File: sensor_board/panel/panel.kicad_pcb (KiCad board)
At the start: 2 copper layers, 102.6 x 105.2 mm, 132 parts, among them J1 Comm, J2 OUTPUT, J3 INPUT, U1 INA228

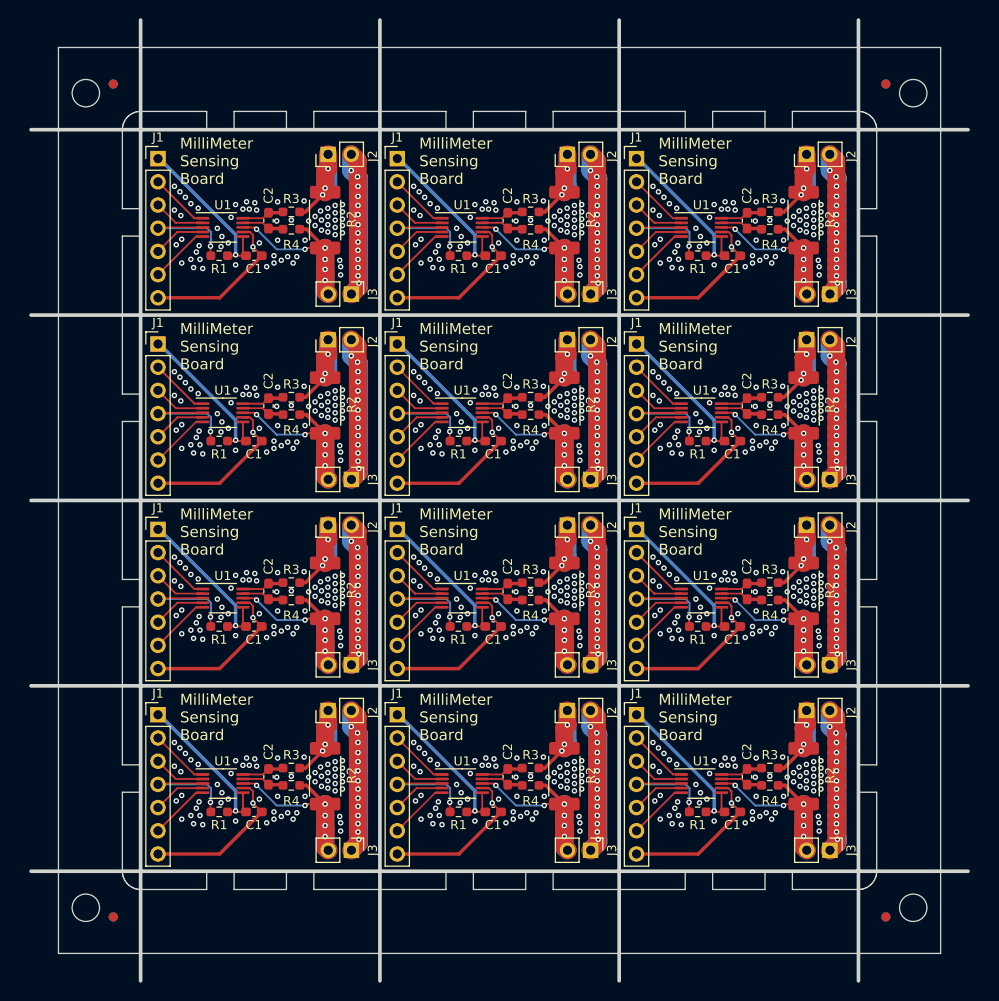
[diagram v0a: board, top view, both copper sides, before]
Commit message: sensor_board: rev 1.1
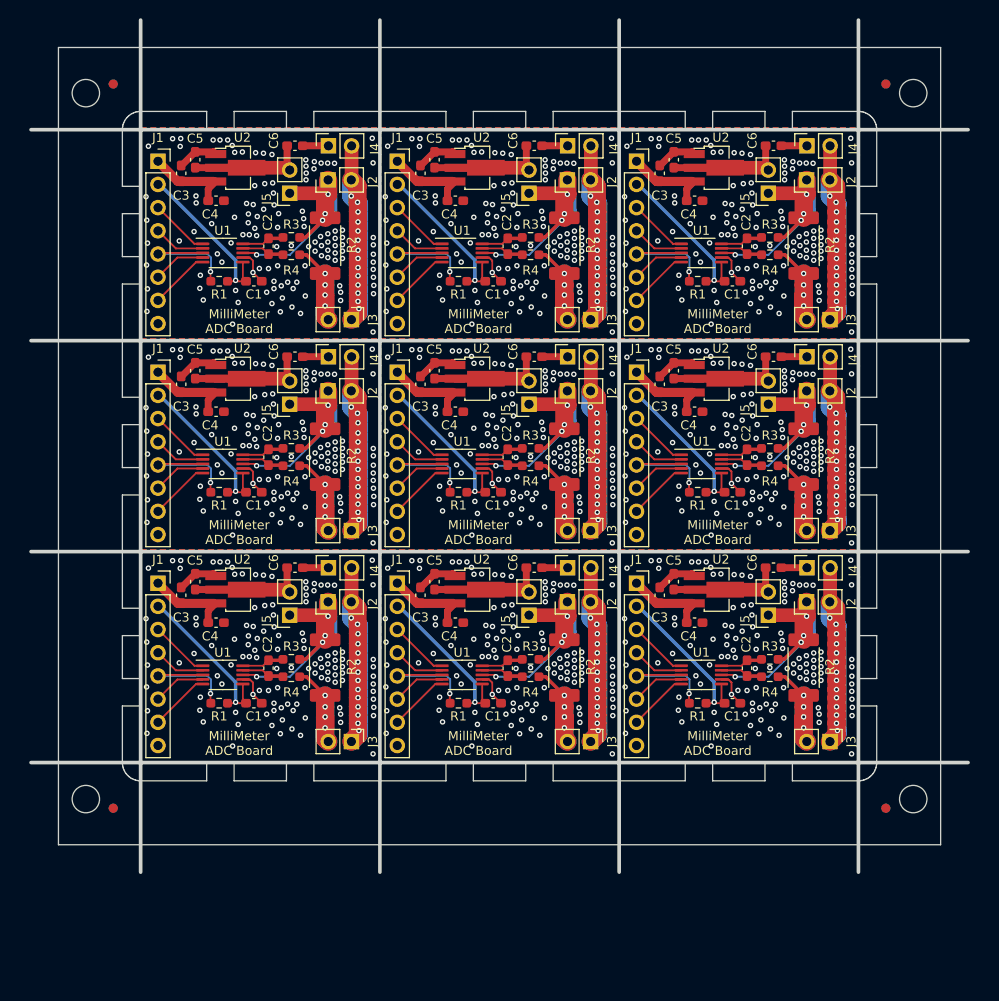
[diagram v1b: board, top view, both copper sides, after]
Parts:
- removed the C1 at (174.0, 63.1)
- removed the C1 at (174.0, 103.7)
- removed the C1 at (147.8, 42.8)
- removed the C1 at (174.0, 42.8)
- removed the C1 at (174.0, 83.4)
- removed the C1 at (121.6, 42.8)
- removed the C1 at (147.8, 83.4)
- removed the C1 at (121.6, 83.4)
- removed the C1 at (147.8, 103.7)
- removed the C1 at (147.8, 63.1)
- removed the C1 at (121.6, 63.1)
- removed the C1 at (121.6, 103.7)
- removed the C2 at (149.4, 99.9)
- removed the C2 at (123.2, 39.0)
- removed the C2 at (123.2, 99.9)
- removed the C2 at (149.4, 39.0)
- removed the C2 at (123.2, 59.3)
- removed the C2 at (175.6, 79.6)
- removed the C2 at (175.6, 39.0)
- removed the C2 at (149.4, 79.6)
- removed the C2 at (175.6, 59.3)
- removed the C2 at (175.6, 99.9)
- removed the C2 at (149.4, 59.3)
- removed the C2 at (123.2, 79.6)
- removed the J1 at (137.3, 72.8)
- removed the J1 at (163.5, 93.1)
- removed the J1 at (137.3, 32.2)
- removed the J1 at (163.5, 32.2)
- removed the J1 at (163.5, 72.8)
- removed the J1 at (111.1, 32.2)
- removed the J1 at (137.3, 52.5)
- removed the J1 at (137.3, 93.1)
- removed the J1 at (163.5, 52.5)
- removed the J1 at (111.1, 72.8)
- removed the J1 at (111.1, 93.1)
- removed the J1 at (111.1, 52.5)
- removed the J2 at (182.1, 92.6)
- removed the J2 at (129.7, 52.0)
- removed the J2 at (155.9, 52.0)
- removed the J2 at (182.1, 72.3)
- removed the J2 at (182.1, 52.0)
- removed the J2 at (155.9, 72.3)
- removed the J2 at (129.7, 31.7)
- removed the J2 at (155.9, 92.6)
- removed the J2 at (129.7, 92.6)
- removed the J2 at (182.1, 31.7)
- removed the J2 at (155.9, 31.7)
- removed the J2 at (129.7, 72.3)
- removed the J3 at (132.3, 87.6)
- removed the J3 at (184.7, 87.6)
- removed the J3 at (184.7, 47.0)
- removed the J3 at (184.7, 67.3)
- removed the J3 at (132.3, 107.9)
- removed the J3 at (158.5, 87.6)
- removed the J3 at (184.7, 107.9)
- removed the J3 at (158.5, 107.9)
- removed the J3 at (132.3, 67.3)
- removed the J3 at (132.3, 47.0)
- removed the J3 at (158.5, 67.3)
- removed the J3 at (158.5, 47.0)
- removed the R1 at (170.2, 63.1)
- removed the R1 at (117.8, 83.4)
- removed the R1 at (170.2, 103.7)
- removed the R1 at (144.0, 103.7)
- removed the R1 at (117.8, 63.1)
- removed the R1 at (170.2, 83.4)
- removed the R1 at (144.0, 42.8)
- removed the R1 at (117.8, 42.8)
- removed the R1 at (170.2, 42.8)
- removed the R1 at (144.0, 63.1)
- removed the R1 at (144.0, 83.4)
- removed the R1 at (117.8, 103.7)
- removed the R2 at (129.4, 59.2)
- removed the R2 at (129.4, 38.9)
- removed the R2 at (155.6, 99.8)
- removed the R2 at (181.8, 38.9)
- removed the R2 at (155.6, 59.2)
- removed the R2 at (155.6, 79.5)
- removed the R2 at (181.8, 79.5)
- removed the R2 at (181.8, 59.2)
- removed the R2 at (155.6, 38.9)
- removed the R2 at (129.4, 79.5)
- removed the R2 at (181.8, 99.8)
- removed the R2 at (129.4, 99.8)
- removed the R3 at (125.7, 38.0)
- removed the R3 at (125.7, 58.3)
- removed the R3 at (151.9, 78.6)
- removed the R3 at (178.1, 38.0)
- removed the R3 at (125.7, 98.9)
- removed the R3 at (125.7, 78.6)
- removed the R3 at (178.1, 98.9)
- removed the R3 at (151.9, 58.3)
- removed the R3 at (178.1, 78.6)
- removed the R3 at (151.9, 98.9)
- removed the R3 at (151.9, 38.0)
- removed the R3 at (178.1, 58.3)
- removed the R4 at (125.7, 100.8)
- removed the R4 at (178.1, 60.2)
- removed the R4 at (125.7, 80.5)
- removed the R4 at (151.9, 60.2)
- removed the R4 at (125.7, 60.2)
- removed the R4 at (178.1, 80.5)
- removed the R4 at (151.9, 80.5)
- removed the R4 at (178.1, 39.9)
- removed the R4 at (151.9, 39.9)
- removed the R4 at (178.1, 100.8)
- removed the R4 at (151.9, 100.8)
- removed the R4 at (125.7, 39.9)
- removed the REF** at (103.2, 114.2)
- removed the REF** at (106.2, 115.2) (x2)
- removed the REF** at (106.2, 24.0) (x2)
- removed the REF** at (190.8, 115.2) (x2)
- removed the REF** at (190.8, 24.0) (x2)
- removed the REF** at (193.8, 114.2)
- removed the U1 at (118.2, 100.6)
- removed the U1 at (144.4, 60.0)
- removed the U1 at (118.2, 39.7)
- removed the U1 at (118.2, 80.3)
- removed the U1 at (170.6, 60.0)
- removed the U1 at (170.6, 39.7)
- removed the U1 at (144.4, 39.7)
- removed the U1 at (170.6, 80.3)
- removed the U1 at (144.4, 100.6)
- removed the U1 at (118.2, 60.0)
- removed the U1 at (144.4, 80.3)
- removed the U1 at (170.6, 100.6)
- added C1: 100nF, Capacitor_SMD:C_0603_1608Metric_Pad1.08x0.95mm_HandSolder, F.Cu at (147.8, 68.7)
- added C1: 100nF, Capacitor_SMD:C_0603_1608Metric_Pad1.08x0.95mm_HandSolder, F.Cu at (121.6, 68.7)
- added C1: 100nF, Capacitor_SMD:C_0603_1608Metric_Pad1.08x0.95mm_HandSolder, F.Cu at (174.0, 91.8)
- added C1: 100nF, Capacitor_SMD:C_0603_1608Metric_Pad1.08x0.95mm_HandSolder, F.Cu at (174.0, 45.6)
- added C1: 100nF, Capacitor_SMD:C_0603_1608Metric_Pad1.08x0.95mm_HandSolder, F.Cu at (121.6, 91.8)
- added C1: 100nF, Capacitor_SMD:C_0603_1608Metric_Pad1.08x0.95mm_HandSolder, F.Cu at (121.6, 45.6)
- added C1: 100nF, Capacitor_SMD:C_0603_1608Metric_Pad1.08x0.95mm_HandSolder, F.Cu at (147.8, 45.6)
- added C1: 100nF, Capacitor_SMD:C_0603_1608Metric_Pad1.08x0.95mm_HandSolder, F.Cu at (174.0, 68.7)
- added C1: 100nF, Capacitor_SMD:C_0603_1608Metric_Pad1.08x0.95mm_HandSolder, F.Cu at (147.8, 91.8)
- added C2: 100nF, Capacitor_SMD:C_0603_1608Metric_Pad1.08x0.95mm_HandSolder, F.Cu at (175.6, 88.0)
- added C2: 100nF, Capacitor_SMD:C_0603_1608Metric_Pad1.08x0.95mm_HandSolder, F.Cu at (149.4, 64.9)
- added C2: 100nF, Capacitor_SMD:C_0603_1608Metric_Pad1.08x0.95mm_HandSolder, F.Cu at (175.6, 41.8)
- added C2: 100nF, Capacitor_SMD:C_0603_1608Metric_Pad1.08x0.95mm_HandSolder, F.Cu at (175.6, 64.9)
- added C2: 100nF, Capacitor_SMD:C_0603_1608Metric_Pad1.08x0.95mm_HandSolder, F.Cu at (149.4, 88.0)
- added C2: 100nF, Capacitor_SMD:C_0603_1608Metric_Pad1.08x0.95mm_HandSolder, F.Cu at (149.4, 41.8)
- added C2: 100nF, Capacitor_SMD:C_0603_1608Metric_Pad1.08x0.95mm_HandSolder, F.Cu at (123.2, 88.0)
- added C2: 100nF, Capacitor_SMD:C_0603_1608Metric_Pad1.08x0.95mm_HandSolder, F.Cu at (123.2, 64.9)
- added C2: 100nF, Capacitor_SMD:C_0603_1608Metric_Pad1.08x0.95mm_HandSolder, F.Cu at (123.2, 41.8)
- added C3: 10uF, Capacitor_SMD:C_0603_1608Metric_Pad1.08x0.95mm_HandSolder, F.Cu at (113.6, 80.0)
- added C3: 10uF, Capacitor_SMD:C_0603_1608Metric_Pad1.08x0.95mm_HandSolder, F.Cu at (139.8, 56.9)
- added C3: 10uF, Capacitor_SMD:C_0603_1608Metric_Pad1.08x0.95mm_HandSolder, F.Cu at (166.0, 56.9)
- added C3: 10uF, Capacitor_SMD:C_0603_1608Metric_Pad1.08x0.95mm_HandSolder, F.Cu at (113.6, 33.8)
- added C3: 10uF, Capacitor_SMD:C_0603_1608Metric_Pad1.08x0.95mm_HandSolder, F.Cu at (139.8, 80.0)
- added C3: 10uF, Capacitor_SMD:C_0603_1608Metric_Pad1.08x0.95mm_HandSolder, F.Cu at (166.0, 33.8)
- added C3: 10uF, Capacitor_SMD:C_0603_1608Metric_Pad1.08x0.95mm_HandSolder, F.Cu at (166.0, 80.0)
- added C3: 10uF, Capacitor_SMD:C_0603_1608Metric_Pad1.08x0.95mm_HandSolder, F.Cu at (113.6, 56.9)
- added C3: 10uF, Capacitor_SMD:C_0603_1608Metric_Pad1.08x0.95mm_HandSolder, F.Cu at (139.8, 33.8)
- added C4: 0.1uF, Capacitor_SMD:C_0603_1608Metric_Pad1.08x0.95mm_HandSolder, F.Cu at (169.9, 59.9)
- added C4: 0.1uF, Capacitor_SMD:C_0603_1608Metric_Pad1.08x0.95mm_HandSolder, F.Cu at (143.7, 36.8)
- added C4: 0.1uF, Capacitor_SMD:C_0603_1608Metric_Pad1.08x0.95mm_HandSolder, F.Cu at (143.7, 59.9)
- added C4: 0.1uF, Capacitor_SMD:C_0603_1608Metric_Pad1.08x0.95mm_HandSolder, F.Cu at (143.7, 83.0)
- added C4: 0.1uF, Capacitor_SMD:C_0603_1608Metric_Pad1.08x0.95mm_HandSolder, F.Cu at (117.5, 83.0)
- added C4: 0.1uF, Capacitor_SMD:C_0603_1608Metric_Pad1.08x0.95mm_HandSolder, F.Cu at (117.5, 59.9)
- added C4: 0.1uF, Capacitor_SMD:C_0603_1608Metric_Pad1.08x0.95mm_HandSolder, F.Cu at (117.5, 36.8)
- added C4: 0.1uF, Capacitor_SMD:C_0603_1608Metric_Pad1.08x0.95mm_HandSolder, F.Cu at (169.9, 36.8)
- added C4: 0.1uF, Capacitor_SMD:C_0603_1608Metric_Pad1.08x0.95mm_HandSolder, F.Cu at (169.9, 83.0)
- added C5: 0.1uF, Capacitor_SMD:C_0603_1608Metric_Pad1.08x0.95mm_HandSolder, F.Cu at (115.2, 78.5)
- added C5: 0.1uF, Capacitor_SMD:C_0603_1608Metric_Pad1.08x0.95mm_HandSolder, F.Cu at (167.6, 78.5)
- added C5: 0.1uF, Capacitor_SMD:C_0603_1608Metric_Pad1.08x0.95mm_HandSolder, F.Cu at (167.6, 55.4)
- added C5: 0.1uF, Capacitor_SMD:C_0603_1608Metric_Pad1.08x0.95mm_HandSolder, F.Cu at (141.4, 55.4)
- added C5: 0.1uF, Capacitor_SMD:C_0603_1608Metric_Pad1.08x0.95mm_HandSolder, F.Cu at (167.6, 32.3)
- added C5: 0.1uF, Capacitor_SMD:C_0603_1608Metric_Pad1.08x0.95mm_HandSolder, F.Cu at (141.4, 78.5)
- added C5: 0.1uF, Capacitor_SMD:C_0603_1608Metric_Pad1.08x0.95mm_HandSolder, F.Cu at (141.4, 32.3)
- added C5: 0.1uF, Capacitor_SMD:C_0603_1608Metric_Pad1.08x0.95mm_HandSolder, F.Cu at (115.2, 32.3)
- added C5: 0.1uF, Capacitor_SMD:C_0603_1608Metric_Pad1.08x0.95mm_HandSolder, F.Cu at (115.2, 55.4)
- added C6: 10uF, Capacitor_SMD:C_0603_1608Metric_Pad1.08x0.95mm_HandSolder, F.Cu at (152.3, 53.9)
- added C6: 10uF, Capacitor_SMD:C_0603_1608Metric_Pad1.08x0.95mm_HandSolder, F.Cu at (152.3, 30.8)
- added C6: 10uF, Capacitor_SMD:C_0603_1608Metric_Pad1.08x0.95mm_HandSolder, F.Cu at (178.5, 30.8)
- added C6: 10uF, Capacitor_SMD:C_0603_1608Metric_Pad1.08x0.95mm_HandSolder, F.Cu at (152.3, 77.0)
- added C6: 10uF, Capacitor_SMD:C_0603_1608Metric_Pad1.08x0.95mm_HandSolder, F.Cu at (178.5, 77.0)
- added C6: 10uF, Capacitor_SMD:C_0603_1608Metric_Pad1.08x0.95mm_HandSolder, F.Cu at (126.1, 77.0)
- added C6: 10uF, Capacitor_SMD:C_0603_1608Metric_Pad1.08x0.95mm_HandSolder, F.Cu at (126.1, 30.8)
- added C6: 10uF, Capacitor_SMD:C_0603_1608Metric_Pad1.08x0.95mm_HandSolder, F.Cu at (126.1, 53.9)
- added C6: 10uF, Capacitor_SMD:C_0603_1608Metric_Pad1.08x0.95mm_HandSolder, F.Cu at (178.5, 53.9)
- added J1: Comm, Connector_PinSocket_2.54mm:PinSocket_1x08_P2.54mm_Vertical, F.Cu at (163.5, 78.7)
- added J1: Comm, Connector_PinSocket_2.54mm:PinSocket_1x08_P2.54mm_Vertical, F.Cu at (111.1, 78.7)
- added J1: Comm, Connector_PinSocket_2.54mm:PinSocket_1x08_P2.54mm_Vertical, F.Cu at (137.3, 78.7)
- added J1: Comm, Connector_PinSocket_2.54mm:PinSocket_1x08_P2.54mm_Vertical, F.Cu at (137.3, 55.6)
- added J1: Comm, Connector_PinSocket_2.54mm:PinSocket_1x08_P2.54mm_Vertical, F.Cu at (163.5, 55.6)
- added J1: Comm, Connector_PinSocket_2.54mm:PinSocket_1x08_P2.54mm_Vertical, F.Cu at (111.1, 32.5)
- added J1: Comm, Connector_PinSocket_2.54mm:PinSocket_1x08_P2.54mm_Vertical, F.Cu at (111.1, 55.6)
- added J1: Comm, Connector_PinSocket_2.54mm:PinSocket_1x08_P2.54mm_Vertical, F.Cu at (163.5, 32.5)
- added J1: Comm, Connector_PinSocket_2.54mm:PinSocket_1x08_P2.54mm_Vertical, F.Cu at (137.3, 32.5)
- added J2: OUTPUT, Connector_PinHeader_2.54mm:PinHeader_1x02_P2.54mm_Vertical, F.Cu at (129.7, 80.7)
- added J2: OUTPUT, Connector_PinHeader_2.54mm:PinHeader_1x02_P2.54mm_Vertical, F.Cu at (155.9, 34.5)
- added J2: OUTPUT, Connector_PinHeader_2.54mm:PinHeader_1x02_P2.54mm_Vertical, F.Cu at (182.1, 80.7)
- added J2: OUTPUT, Connector_PinHeader_2.54mm:PinHeader_1x02_P2.54mm_Vertical, F.Cu at (182.1, 57.6)
- added J2: OUTPUT, Connector_PinHeader_2.54mm:PinHeader_1x02_P2.54mm_Vertical, F.Cu at (155.9, 57.6)
- added J2: OUTPUT, Connector_PinHeader_2.54mm:PinHeader_1x02_P2.54mm_Vertical, F.Cu at (155.9, 80.7)
- added J2: OUTPUT, Connector_PinHeader_2.54mm:PinHeader_1x02_P2.54mm_Vertical, F.Cu at (129.7, 34.5)
- added J2: OUTPUT, Connector_PinHeader_2.54mm:PinHeader_1x02_P2.54mm_Vertical, F.Cu at (129.7, 57.6)
- added J2: OUTPUT, Connector_PinHeader_2.54mm:PinHeader_1x02_P2.54mm_Vertical, F.Cu at (182.1, 34.5)
- added J3: INPUT, Connector_PinHeader_2.54mm:PinHeader_1x02_P2.54mm_Vertical, F.Cu at (132.3, 72.9)
- added J3: INPUT, Connector_PinHeader_2.54mm:PinHeader_1x02_P2.54mm_Vertical, F.Cu at (184.7, 96.0)
- added J3: INPUT, Connector_PinHeader_2.54mm:PinHeader_1x02_P2.54mm_Vertical, F.Cu at (158.5, 49.8)
- added J3: INPUT, Connector_PinHeader_2.54mm:PinHeader_1x02_P2.54mm_Vertical, F.Cu at (132.3, 96.0)
- added J3: INPUT, Connector_PinHeader_2.54mm:PinHeader_1x02_P2.54mm_Vertical, F.Cu at (132.3, 49.8)
- added J3: INPUT, Connector_PinHeader_2.54mm:PinHeader_1x02_P2.54mm_Vertical, F.Cu at (184.7, 72.9)
- added J3: INPUT, Connector_PinHeader_2.54mm:PinHeader_1x02_P2.54mm_Vertical, F.Cu at (158.5, 72.9)
- added J3: INPUT, Connector_PinHeader_2.54mm:PinHeader_1x02_P2.54mm_Vertical, F.Cu at (158.5, 96.0)
- added J3: INPUT, Connector_PinHeader_2.54mm:PinHeader_1x02_P2.54mm_Vertical, F.Cu at (184.7, 49.8)
- added J4: LDO_GND, Connector_PinSocket_2.54mm:PinSocket_1x02_P2.54mm_Vertical, F.Cu at (129.8, 53.9)
- added J4: LDO_GND, Connector_PinSocket_2.54mm:PinSocket_1x02_P2.54mm_Vertical, F.Cu at (182.2, 30.8)
- added J4: LDO_GND, Connector_PinSocket_2.54mm:PinSocket_1x02_P2.54mm_Vertical, F.Cu at (129.8, 77.0)
- added J4: LDO_GND, Connector_PinSocket_2.54mm:PinSocket_1x02_P2.54mm_Vertical, F.Cu at (156.0, 30.8)
- added J4: LDO_GND, Connector_PinSocket_2.54mm:PinSocket_1x02_P2.54mm_Vertical, F.Cu at (129.8, 30.8)
- added J4: LDO_GND, Connector_PinSocket_2.54mm:PinSocket_1x02_P2.54mm_Vertical, F.Cu at (182.2, 77.0)
- added J4: LDO_GND, Connector_PinSocket_2.54mm:PinSocket_1x02_P2.54mm_Vertical, F.Cu at (156.0, 53.9)
- added J4: LDO_GND, Connector_PinSocket_2.54mm:PinSocket_1x02_P2.54mm_Vertical, F.Cu at (182.2, 53.9)
- added J4: LDO_GND, Connector_PinSocket_2.54mm:PinSocket_1x02_P2.54mm_Vertical, F.Cu at (156.0, 77.0)
- added J5: LDO_VCC, Connector_PinSocket_2.54mm:PinSocket_1x02_P2.54mm_Vertical, F.Cu at (125.5, 82.2)
- added J5: LDO_VCC, Connector_PinSocket_2.54mm:PinSocket_1x02_P2.54mm_Vertical, F.Cu at (125.5, 59.1)
- added J5: LDO_VCC, Connector_PinSocket_2.54mm:PinSocket_1x02_P2.54mm_Vertical, F.Cu at (151.7, 82.2)
- added J5: LDO_VCC, Connector_PinSocket_2.54mm:PinSocket_1x02_P2.54mm_Vertical, F.Cu at (177.9, 82.2)
- added J5: LDO_VCC, Connector_PinSocket_2.54mm:PinSocket_1x02_P2.54mm_Vertical, F.Cu at (177.9, 36.0)
- added J5: LDO_VCC, Connector_PinSocket_2.54mm:PinSocket_1x02_P2.54mm_Vertical, F.Cu at (151.7, 59.1)
- added J5: LDO_VCC, Connector_PinSocket_2.54mm:PinSocket_1x02_P2.54mm_Vertical, F.Cu at (151.7, 36.0)
- added J5: LDO_VCC, Connector_PinSocket_2.54mm:PinSocket_1x02_P2.54mm_Vertical, F.Cu at (177.9, 59.1)
- added J5: LDO_VCC, Connector_PinSocket_2.54mm:PinSocket_1x02_P2.54mm_Vertical, F.Cu at (125.5, 36.0)
- added R1: 10k, Resistor_SMD:R_0603_1608Metric_Pad0.98x0.95mm_HandSolder, F.Cu at (170.2, 91.8)
- added R1: 10k, Resistor_SMD:R_0603_1608Metric_Pad0.98x0.95mm_HandSolder, F.Cu at (117.8, 45.6)
- added R1: 10k, Resistor_SMD:R_0603_1608Metric_Pad0.98x0.95mm_HandSolder, F.Cu at (117.8, 68.7)
- added R1: 10k, Resistor_SMD:R_0603_1608Metric_Pad0.98x0.95mm_HandSolder, F.Cu at (117.8, 91.8)
- added R1: 10k, Resistor_SMD:R_0603_1608Metric_Pad0.98x0.95mm_HandSolder, F.Cu at (170.2, 68.7)
- added R1: 10k, Resistor_SMD:R_0603_1608Metric_Pad0.98x0.95mm_HandSolder, F.Cu at (144.0, 45.6)
- added R1: 10k, Resistor_SMD:R_0603_1608Metric_Pad0.98x0.95mm_HandSolder, F.Cu at (170.2, 45.6)
- added R1: 10k, Resistor_SMD:R_0603_1608Metric_Pad0.98x0.95mm_HandSolder, F.Cu at (144.0, 91.8)
- added R1: 10k, Resistor_SMD:R_0603_1608Metric_Pad0.98x0.95mm_HandSolder, F.Cu at (144.0, 68.7)
- added R2: 0.05R, Resistor_SMD:R_2512_6332Metric_Pad1.40x3.35mm_HandSolder, F.Cu at (129.4, 41.7)
- added R2: 0.05R, Resistor_SMD:R_2512_6332Metric_Pad1.40x3.35mm_HandSolder, F.Cu at (181.8, 87.9)
- added R2: 0.05R, Resistor_SMD:R_2512_6332Metric_Pad1.40x3.35mm_HandSolder, F.Cu at (129.4, 87.9)
- added R2: 0.05R, Resistor_SMD:R_2512_6332Metric_Pad1.40x3.35mm_HandSolder, F.Cu at (155.6, 41.7)
- added R2: 0.05R, Resistor_SMD:R_2512_6332Metric_Pad1.40x3.35mm_HandSolder, F.Cu at (181.8, 41.7)
- added R2: 0.05R, Resistor_SMD:R_2512_6332Metric_Pad1.40x3.35mm_HandSolder, F.Cu at (181.8, 64.8)
- added R2: 0.05R, Resistor_SMD:R_2512_6332Metric_Pad1.40x3.35mm_HandSolder, F.Cu at (155.6, 87.9)
- added R2: 0.05R, Resistor_SMD:R_2512_6332Metric_Pad1.40x3.35mm_HandSolder, F.Cu at (129.4, 64.8)
- added R2: 0.05R, Resistor_SMD:R_2512_6332Metric_Pad1.40x3.35mm_HandSolder, F.Cu at (155.6, 64.8)
- added R3: 47R, Resistor_SMD:R_0603_1608Metric_Pad0.98x0.95mm_HandSolder, F.Cu at (151.9, 87.0)
- added R3: 47R, Resistor_SMD:R_0603_1608Metric_Pad0.98x0.95mm_HandSolder, F.Cu at (151.9, 40.8)
- added R3: 47R, Resistor_SMD:R_0603_1608Metric_Pad0.98x0.95mm_HandSolder, F.Cu at (125.7, 63.9)
- added R3: 47R, Resistor_SMD:R_0603_1608Metric_Pad0.98x0.95mm_HandSolder, F.Cu at (178.1, 40.8)
- added R3: 47R, Resistor_SMD:R_0603_1608Metric_Pad0.98x0.95mm_HandSolder, F.Cu at (178.1, 87.0)
- added R3: 47R, Resistor_SMD:R_0603_1608Metric_Pad0.98x0.95mm_HandSolder, F.Cu at (151.9, 63.9)
- added R3: 47R, Resistor_SMD:R_0603_1608Metric_Pad0.98x0.95mm_HandSolder, F.Cu at (178.1, 63.9)
- added R3: 47R, Resistor_SMD:R_0603_1608Metric_Pad0.98x0.95mm_HandSolder, F.Cu at (125.7, 87.0)
- added R3: 47R, Resistor_SMD:R_0603_1608Metric_Pad0.98x0.95mm_HandSolder, F.Cu at (125.7, 40.8)
- added R4: 47R, Resistor_SMD:R_0603_1608Metric_Pad0.98x0.95mm_HandSolder, F.Cu at (178.1, 88.9)
- added R4: 47R, Resistor_SMD:R_0603_1608Metric_Pad0.98x0.95mm_HandSolder, F.Cu at (125.7, 42.7)
- added R4: 47R, Resistor_SMD:R_0603_1608Metric_Pad0.98x0.95mm_HandSolder, F.Cu at (151.9, 42.7)
- added R4: 47R, Resistor_SMD:R_0603_1608Metric_Pad0.98x0.95mm_HandSolder, F.Cu at (125.7, 88.9)
- added R4: 47R, Resistor_SMD:R_0603_1608Metric_Pad0.98x0.95mm_HandSolder, F.Cu at (151.9, 88.9)
- added R4: 47R, Resistor_SMD:R_0603_1608Metric_Pad0.98x0.95mm_HandSolder, F.Cu at (151.9, 65.8)
- added R4: 47R, Resistor_SMD:R_0603_1608Metric_Pad0.98x0.95mm_HandSolder, F.Cu at (178.1, 65.8)
- added R4: 47R, Resistor_SMD:R_0603_1608Metric_Pad0.98x0.95mm_HandSolder, F.Cu at (125.7, 65.8)
- added R4: 47R, Resistor_SMD:R_0603_1608Metric_Pad0.98x0.95mm_HandSolder, F.Cu at (178.1, 42.7)
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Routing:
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- removed copper zone on B.Cu, net Board_10-GND
- removed copper zone on F.Cu, net Board_10-GND
- removed copper zone on B.Cu, net Board_11-GND
- removed copper zone on F.Cu, net Board_11-GND
- removed copper zone on B.Cu, net Board_9-GND
- removed copper zone on F.Cu, net Board_9-GND
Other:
- board size 102.6 x 105.2 mm -> 102.6 x 93.3 mm
- board text added: "<<<<<<<<"
- board text added: "Copyright (C) 2023 Jackson M Hu Rev 1"
- board text added: "LDO_GND"
- board text added: "LDO_Vext"
- board text added: "MilliMeter ADC Board"
- board text added: "Vext 3v3 A1 A0 ALERT SDA SCL GND"
- board text removed: "(C) 2022 Jackson M Hu Rev 1"
- board text removed: "---->>"
- board text removed: "3v3 A1 A0 ALERT SDA SCL GND"
- board text removed: "MilliMeter Sensing Board"

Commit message: Generate Rev. 1 gerber
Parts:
- removed the C1 at (147.8, 68.7)
- removed the C1 at (121.6, 68.7)
- removed the C1 at (174.0, 91.8)
- removed the C1 at (174.0, 45.6)
- removed the C1 at (121.6, 91.8)
- removed the C1 at (121.6, 45.6)
- removed the C1 at (174.0, 68.7)
- removed the C1 at (147.8, 91.8)
- removed the C2 at (175.6, 88.0)
- removed the C2 at (149.4, 64.9)
- removed the C2 at (175.6, 41.8)
- removed the C2 at (175.6, 64.9)
- removed the C2 at (149.4, 88.0)
- removed the C2 at (123.2, 88.0)
- removed the C2 at (123.2, 64.9)
- removed the C2 at (123.2, 41.8)
- removed the C3 at (113.6, 80.0)
- removed the C3 at (139.8, 56.9)
- removed the C3 at (166.0, 56.9)
- removed the C3 at (113.6, 33.8)
- removed the C3 at (139.8, 80.0)
- removed the C3 at (166.0, 33.8)
- removed the C3 at (166.0, 80.0)
- removed the C3 at (113.6, 56.9)
- removed the C4 at (169.9, 59.9)
- removed the C4 at (143.7, 59.9)
- removed the C4 at (143.7, 83.0)
- removed the C4 at (117.5, 83.0)
- removed the C4 at (117.5, 59.9)
- removed the C4 at (117.5, 36.8)
- removed the C4 at (169.9, 36.8)
- removed the C4 at (169.9, 83.0)
- removed the C5 at (115.2, 78.5)
- removed the C5 at (167.6, 78.5)
- removed the C5 at (167.6, 55.4)
- removed the C5 at (141.4, 55.4)
- removed the C5 at (167.6, 32.3)
- removed the C5 at (141.4, 78.5)
- removed the C5 at (115.2, 32.3)
- removed the C5 at (115.2, 55.4)
- removed the C6 at (152.3, 53.9)
- removed the C6 at (178.5, 30.8)
- removed the C6 at (152.3, 77.0)
- removed the C6 at (178.5, 77.0)
- removed the C6 at (126.1, 77.0)
- removed the C6 at (126.1, 30.8)
- removed the C6 at (126.1, 53.9)
- removed the C6 at (178.5, 53.9)
- removed the J1 at (163.5, 78.7)
- removed the J1 at (111.1, 78.7)
- removed the J1 at (137.3, 78.7)
- removed the J1 at (137.3, 55.6)
- removed the J1 at (163.5, 55.6)
- removed the J1 at (111.1, 32.5)
- removed the J1 at (111.1, 55.6)
- removed the J1 at (163.5, 32.5)
- removed the J2 at (129.7, 80.7)
- removed the J2 at (182.1, 80.7)
- removed the J2 at (182.1, 57.6)
- removed the J2 at (155.9, 57.6)
- removed the J2 at (155.9, 80.7)
- removed the J2 at (129.7, 34.5)
- removed the J2 at (129.7, 57.6)
- removed the J2 at (182.1, 34.5)
- removed the J3 at (132.3, 72.9)
- removed the J3 at (184.7, 96.0)
- removed the J3 at (132.3, 96.0)
- removed the J3 at (132.3, 49.8)
- removed the J3 at (184.7, 72.9)
- removed the J3 at (158.5, 72.9)
- removed the J3 at (158.5, 96.0)
- removed the J3 at (184.7, 49.8)
- removed the J4 at (129.8, 53.9)
- removed the J4 at (182.2, 30.8)
- removed the J4 at (129.8, 77.0)
- removed the J4 at (129.8, 30.8)
- removed the J4 at (182.2, 77.0)
- removed the J4 at (156.0, 53.9)
- removed the J4 at (182.2, 53.9)
- removed the J4 at (156.0, 77.0)
- removed the J5 at (125.5, 82.2)
- removed the J5 at (125.5, 59.1)
- removed the J5 at (151.7, 82.2)
- removed the J5 at (177.9, 82.2)
- removed the J5 at (177.9, 36.0)
- removed the J5 at (151.7, 59.1)
- removed the J5 at (177.9, 59.1)
- removed the J5 at (125.5, 36.0)
- removed the R1 at (170.2, 91.8)
- removed the R1 at (117.8, 45.6)
- removed the R1 at (117.8, 68.7)
- removed the R1 at (117.8, 91.8)
- removed the R1 at (170.2, 68.7)
- removed the R1 at (170.2, 45.6)
- removed the R1 at (144.0, 91.8)
- removed the R1 at (144.0, 68.7)
- removed the R2 at (129.4, 41.7)
- removed the R2 at (181.8, 87.9)
- removed the R2 at (129.4, 87.9)
- removed the R2 at (181.8, 41.7)
- removed the R2 at (181.8, 64.8)
- removed the R2 at (155.6, 87.9)
- removed the R2 at (129.4, 64.8)
- removed the R2 at (155.6, 64.8)
- removed the R3 at (151.9, 87.0)
- removed the R3 at (125.7, 63.9)
- removed the R3 at (178.1, 40.8)
- removed the R3 at (178.1, 87.0)
- removed the R3 at (151.9, 63.9)
- removed the R3 at (178.1, 63.9)
- removed the R3 at (125.7, 87.0)
- removed the R3 at (125.7, 40.8)
- removed the R4 at (178.1, 88.9)
- removed the R4 at (125.7, 42.7)
- removed the R4 at (125.7, 88.9)
- removed the R4 at (151.9, 88.9)
- removed the R4 at (151.9, 65.8)
- removed the R4 at (178.1, 65.8)
- removed the R4 at (125.7, 65.8)
- removed the R4 at (178.1, 42.7)
- removed the REF** at (103.2, 25.0)
- removed the REF** at (106.2, 103.3) (x2)
- removed the REF** at (106.2, 24.0) (x2)
- removed the REF** at (190.8, 24.0) (x2)
- removed the REF** at (193.8, 102.3)
- removed the REF** at (193.8, 25.0)
- removed the REF** at (190.8, 103.3) (x2)
- removed the REF** at (103.2, 102.3)
- removed the U1 at (144.4, 65.6)
- removed the U1 at (118.2, 65.6)
- removed the U1 at (170.6, 42.5)
- removed the U1 at (170.6, 88.7)
- removed the U1 at (118.2, 88.7)
- removed the U1 at (118.2, 42.5)
- removed the U1 at (144.4, 88.7)
- removed the U1 at (170.6, 65.6)
- removed the U2 at (145.8, 56.3)
- removed the U2 at (172.0, 33.2)
- removed the U2 at (119.6, 56.3)
- removed the U2 at (145.8, 79.4)
- removed the U2 at (172.0, 56.3)
- removed the U2 at (119.6, 79.4)
- removed the U2 at (119.6, 33.2)
- removed the U2 at (172.0, 79.4)
- added C1: 100nF, Capacitor_SMD:C_0603_1608Metric_Pad1.08x0.95mm_HandSolder, F.Cu at (147.8, 69.6)
- added C1: 100nF, Capacitor_SMD:C_0603_1608Metric_Pad1.08x0.95mm_HandSolder, F.Cu at (147.8, 93.6)
- added C1: 100nF, Capacitor_SMD:C_0603_1608Metric_Pad1.08x0.95mm_HandSolder, F.Cu at (120.8, 45.6)
- added C1: 100nF, Capacitor_SMD:C_0603_1608Metric_Pad1.08x0.95mm_HandSolder, F.Cu at (174.8, 45.6)
- added C1: 100nF, Capacitor_SMD:C_0603_1608Metric_Pad1.08x0.95mm_HandSolder, F.Cu at (120.8, 93.6)
- added C1: 100nF, Capacitor_SMD:C_0603_1608Metric_Pad1.08x0.95mm_HandSolder, F.Cu at (174.8, 69.6)
- added C1: 100nF, Capacitor_SMD:C_0603_1608Metric_Pad1.08x0.95mm_HandSolder, F.Cu at (174.8, 93.6)
- added C1: 100nF, Capacitor_SMD:C_0603_1608Metric_Pad1.08x0.95mm_HandSolder, F.Cu at (120.8, 69.6)
- added C2: 100nF, Capacitor_SMD:C_0603_1608Metric_Pad1.08x0.95mm_HandSolder, F.Cu at (149.4, 65.8)
- added C2: 100nF, Capacitor_SMD:C_0603_1608Metric_Pad1.08x0.95mm_HandSolder, F.Cu at (176.4, 65.8)
- added C2: 100nF, Capacitor_SMD:C_0603_1608Metric_Pad1.08x0.95mm_HandSolder, F.Cu at (122.4, 41.8)
- added C2: 100nF, Capacitor_SMD:C_0603_1608Metric_Pad1.08x0.95mm_HandSolder, F.Cu at (122.4, 65.8)
- added C2: 100nF, Capacitor_SMD:C_0603_1608Metric_Pad1.08x0.95mm_HandSolder, F.Cu at (122.4, 89.8)
- added C2: 100nF, Capacitor_SMD:C_0603_1608Metric_Pad1.08x0.95mm_HandSolder, F.Cu at (176.4, 41.8)
- added C2: 100nF, Capacitor_SMD:C_0603_1608Metric_Pad1.08x0.95mm_HandSolder, F.Cu at (149.4, 89.8)
- added C2: 100nF, Capacitor_SMD:C_0603_1608Metric_Pad1.08x0.95mm_HandSolder, F.Cu at (176.4, 89.8)
- added C3: 10uF, Capacitor_SMD:C_0603_1608Metric_Pad1.08x0.95mm_HandSolder, F.Cu at (112.8, 57.8)
- added C3: 10uF, Capacitor_SMD:C_0603_1608Metric_Pad1.08x0.95mm_HandSolder, F.Cu at (166.8, 81.8)
- added C3: 10uF, Capacitor_SMD:C_0603_1608Metric_Pad1.08x0.95mm_HandSolder, F.Cu at (166.8, 33.8)
- added C3: 10uF, Capacitor_SMD:C_0603_1608Metric_Pad1.08x0.95mm_HandSolder, F.Cu at (166.8, 57.8)
- added C3: 10uF, Capacitor_SMD:C_0603_1608Metric_Pad1.08x0.95mm_HandSolder, F.Cu at (139.8, 81.8)
- added C3: 10uF, Capacitor_SMD:C_0603_1608Metric_Pad1.08x0.95mm_HandSolder, F.Cu at (112.8, 81.8)
- added C3: 10uF, Capacitor_SMD:C_0603_1608Metric_Pad1.08x0.95mm_HandSolder, F.Cu at (112.8, 33.8)
- added C3: 10uF, Capacitor_SMD:C_0603_1608Metric_Pad1.08x0.95mm_HandSolder, F.Cu at (139.8, 57.8)
- added C4: 0.1uF, Capacitor_SMD:C_0603_1608Metric_Pad1.08x0.95mm_HandSolder, F.Cu at (170.7, 36.8)
- added C4: 0.1uF, Capacitor_SMD:C_0603_1608Metric_Pad1.08x0.95mm_HandSolder, F.Cu at (170.7, 60.8)
- added C4: 0.1uF, Capacitor_SMD:C_0603_1608Metric_Pad1.08x0.95mm_HandSolder, F.Cu at (116.7, 36.8)
- added C4: 0.1uF, Capacitor_SMD:C_0603_1608Metric_Pad1.08x0.95mm_HandSolder, F.Cu at (143.7, 60.8)
- added C4: 0.1uF, Capacitor_SMD:C_0603_1608Metric_Pad1.08x0.95mm_HandSolder, F.Cu at (116.7, 60.8)
- added C4: 0.1uF, Capacitor_SMD:C_0603_1608Metric_Pad1.08x0.95mm_HandSolder, F.Cu at (143.7, 84.8)
- added C4: 0.1uF, Capacitor_SMD:C_0603_1608Metric_Pad1.08x0.95mm_HandSolder, F.Cu at (116.7, 84.8)
- added C4: 0.1uF, Capacitor_SMD:C_0603_1608Metric_Pad1.08x0.95mm_HandSolder, F.Cu at (170.7, 84.8)
- added C5: 0.1uF, Capacitor_SMD:C_0603_1608Metric_Pad1.08x0.95mm_HandSolder, F.Cu at (168.4, 80.3)
- added C5: 0.1uF, Capacitor_SMD:C_0603_1608Metric_Pad1.08x0.95mm_HandSolder, F.Cu at (114.4, 80.3)
- added C5: 0.1uF, Capacitor_SMD:C_0603_1608Metric_Pad1.08x0.95mm_HandSolder, F.Cu at (168.4, 56.3)
- added C5: 0.1uF, Capacitor_SMD:C_0603_1608Metric_Pad1.08x0.95mm_HandSolder, F.Cu at (141.4, 56.3)
- added C5: 0.1uF, Capacitor_SMD:C_0603_1608Metric_Pad1.08x0.95mm_HandSolder, F.Cu at (114.4, 56.3)
- added C5: 0.1uF, Capacitor_SMD:C_0603_1608Metric_Pad1.08x0.95mm_HandSolder, F.Cu at (168.4, 32.3)
- added C5: 0.1uF, Capacitor_SMD:C_0603_1608Metric_Pad1.08x0.95mm_HandSolder, F.Cu at (141.4, 80.3)
- added C5: 0.1uF, Capacitor_SMD:C_0603_1608Metric_Pad1.08x0.95mm_HandSolder, F.Cu at (114.4, 32.3)
- added C6: 10uF, Capacitor_SMD:C_0603_1608Metric_Pad1.08x0.95mm_HandSolder, F.Cu at (152.3, 54.8)
- added C6: 10uF, Capacitor_SMD:C_0603_1608Metric_Pad1.08x0.95mm_HandSolder, F.Cu at (125.3, 78.8)
- added C6: 10uF, Capacitor_SMD:C_0603_1608Metric_Pad1.08x0.95mm_HandSolder, F.Cu at (179.3, 78.8)
- added C6: 10uF, Capacitor_SMD:C_0603_1608Metric_Pad1.08x0.95mm_HandSolder, F.Cu at (152.3, 78.8)
- added C6: 10uF, Capacitor_SMD:C_0603_1608Metric_Pad1.08x0.95mm_HandSolder, F.Cu at (179.3, 30.8)
- added C6: 10uF, Capacitor_SMD:C_0603_1608Metric_Pad1.08x0.95mm_HandSolder, F.Cu at (125.3, 30.8)
- added C6: 10uF, Capacitor_SMD:C_0603_1608Metric_Pad1.08x0.95mm_HandSolder, F.Cu at (125.3, 54.8)
- added C6: 10uF, Capacitor_SMD:C_0603_1608Metric_Pad1.08x0.95mm_HandSolder, F.Cu at (179.3, 54.8)
- added J1: Comm, Connector_PinSocket_2.54mm:PinSocket_1x08_P2.54mm_Vertical, F.Cu at (137.3, 56.5)
- added J1: Comm, Connector_PinSocket_2.54mm:PinSocket_1x08_P2.54mm_Vertical, F.Cu at (110.3, 32.5)
- added J1: Comm, Connector_PinSocket_2.54mm:PinSocket_1x08_P2.54mm_Vertical, F.Cu at (110.3, 80.5)
- added J1: Comm, Connector_PinSocket_2.54mm:PinSocket_1x08_P2.54mm_Vertical, F.Cu at (110.3, 56.5)
- added J1: Comm, Connector_PinSocket_2.54mm:PinSocket_1x08_P2.54mm_Vertical, F.Cu at (164.3, 56.5)
- added J1: Comm, Connector_PinSocket_2.54mm:PinSocket_1x08_P2.54mm_Vertical, F.Cu at (137.3, 80.5)
- added J1: Comm, Connector_PinSocket_2.54mm:PinSocket_1x08_P2.54mm_Vertical, F.Cu at (164.3, 32.5)
- added J1: Comm, Connector_PinSocket_2.54mm:PinSocket_1x08_P2.54mm_Vertical, F.Cu at (164.3, 80.5)
- added J2: OUTPUT, Connector_PinHeader_2.54mm:PinHeader_1x02_P2.54mm_Vertical, F.Cu at (128.9, 82.5)
- added J2: OUTPUT, Connector_PinHeader_2.54mm:PinHeader_1x02_P2.54mm_Vertical, F.Cu at (182.9, 34.5)
- added J2: OUTPUT, Connector_PinHeader_2.54mm:PinHeader_1x02_P2.54mm_Vertical, F.Cu at (155.9, 82.5)
- added J2: OUTPUT, Connector_PinHeader_2.54mm:PinHeader_1x02_P2.54mm_Vertical, F.Cu at (182.9, 58.5)
- added J2: OUTPUT, Connector_PinHeader_2.54mm:PinHeader_1x02_P2.54mm_Vertical, F.Cu at (128.9, 58.5)
- added J2: OUTPUT, Connector_PinHeader_2.54mm:PinHeader_1x02_P2.54mm_Vertical, F.Cu at (182.9, 82.5)
- added J2: OUTPUT, Connector_PinHeader_2.54mm:PinHeader_1x02_P2.54mm_Vertical, F.Cu at (155.9, 58.5)
- added J2: OUTPUT, Connector_PinHeader_2.54mm:PinHeader_1x02_P2.54mm_Vertical, F.Cu at (128.9, 34.5)
- added J3: INPUT, Connector_PinHeader_2.54mm:PinHeader_1x02_P2.54mm_Vertical, F.Cu at (185.5, 97.8)
- added J3: INPUT, Connector_PinHeader_2.54mm:PinHeader_1x02_P2.54mm_Vertical, F.Cu at (158.5, 97.8)
- added J3: INPUT, Connector_PinHeader_2.54mm:PinHeader_1x02_P2.54mm_Vertical, F.Cu at (158.5, 73.8)
- added J3: INPUT, Connector_PinHeader_2.54mm:PinHeader_1x02_P2.54mm_Vertical, F.Cu at (185.5, 49.8)
- added J3: INPUT, Connector_PinHeader_2.54mm:PinHeader_1x02_P2.54mm_Vertical, F.Cu at (131.5, 73.8)
- added J3: INPUT, Connector_PinHeader_2.54mm:PinHeader_1x02_P2.54mm_Vertical, F.Cu at (185.5, 73.8)
- added J3: INPUT, Connector_PinHeader_2.54mm:PinHeader_1x02_P2.54mm_Vertical, F.Cu at (131.5, 97.8)
- added J3: INPUT, Connector_PinHeader_2.54mm:PinHeader_1x02_P2.54mm_Vertical, F.Cu at (131.5, 49.8)
- added J4: LDO_GND, Connector_PinSocket_2.54mm:PinSocket_1x02_P2.54mm_Vertical, F.Cu at (156.0, 54.8)
- added J4: LDO_GND, Connector_PinSocket_2.54mm:PinSocket_1x02_P2.54mm_Vertical, F.Cu at (183.0, 78.8)
- added J4: LDO_GND, Connector_PinSocket_2.54mm:PinSocket_1x02_P2.54mm_Vertical, F.Cu at (129.0, 54.8)
- added J4: LDO_GND, Connector_PinSocket_2.54mm:PinSocket_1x02_P2.54mm_Vertical, F.Cu at (129.0, 30.8)
- added J4: LDO_GND, Connector_PinSocket_2.54mm:PinSocket_1x02_P2.54mm_Vertical, F.Cu at (183.0, 54.8)
- added J4: LDO_GND, Connector_PinSocket_2.54mm:PinSocket_1x02_P2.54mm_Vertical, F.Cu at (156.0, 78.8)
- added J4: LDO_GND, Connector_PinSocket_2.54mm:PinSocket_1x02_P2.54mm_Vertical, F.Cu at (129.0, 78.8)
- added J4: LDO_GND, Connector_PinSocket_2.54mm:PinSocket_1x02_P2.54mm_Vertical, F.Cu at (183.0, 30.8)
- added J5: LDO_VCC, Connector_PinSocket_2.54mm:PinSocket_1x02_P2.54mm_Vertical, F.Cu at (151.7, 60.0)
- added J5: LDO_VCC, Connector_PinSocket_2.54mm:PinSocket_1x02_P2.54mm_Vertical, F.Cu at (124.7, 36.0)
- added J5: LDO_VCC, Connector_PinSocket_2.54mm:PinSocket_1x02_P2.54mm_Vertical, F.Cu at (178.7, 36.0)
- added J5: LDO_VCC, Connector_PinSocket_2.54mm:PinSocket_1x02_P2.54mm_Vertical, F.Cu at (124.7, 84.0)
- added J5: LDO_VCC, Connector_PinSocket_2.54mm:PinSocket_1x02_P2.54mm_Vertical, F.Cu at (151.7, 84.0)
- added J5: LDO_VCC, Connector_PinSocket_2.54mm:PinSocket_1x02_P2.54mm_Vertical, F.Cu at (178.7, 60.0)
- added J5: LDO_VCC, Connector_PinSocket_2.54mm:PinSocket_1x02_P2.54mm_Vertical, F.Cu at (178.7, 84.0)
- added J5: LDO_VCC, Connector_PinSocket_2.54mm:PinSocket_1x02_P2.54mm_Vertical, F.Cu at (124.7, 60.0)
- added R1: 10k, Resistor_SMD:R_0603_1608Metric_Pad0.98x0.95mm_HandSolder, F.Cu at (117.0, 93.6)
- added R1: 10k, Resistor_SMD:R_0603_1608Metric_Pad0.98x0.95mm_HandSolder, F.Cu at (171.0, 45.6)
- added R1: 10k, Resistor_SMD:R_0603_1608Metric_Pad0.98x0.95mm_HandSolder, F.Cu at (117.0, 45.6)
- added R1: 10k, Resistor_SMD:R_0603_1608Metric_Pad0.98x0.95mm_HandSolder, F.Cu at (144.0, 69.6)
- added R1: 10k, Resistor_SMD:R_0603_1608Metric_Pad0.98x0.95mm_HandSolder, F.Cu at (171.0, 93.6)
- added R1: 10k, Resistor_SMD:R_0603_1608Metric_Pad0.98x0.95mm_HandSolder, F.Cu at (171.0, 69.6)
- added R1: 10k, Resistor_SMD:R_0603_1608Metric_Pad0.98x0.95mm_HandSolder, F.Cu at (144.0, 93.6)
- added R1: 10k, Resistor_SMD:R_0603_1608Metric_Pad0.98x0.95mm_HandSolder, F.Cu at (117.0, 69.6)
- added R2: 0.05R, Resistor_SMD:R_2512_6332Metric_Pad1.40x3.35mm_HandSolder, F.Cu at (182.6, 89.7)
- added R2: 0.05R, Resistor_SMD:R_2512_6332Metric_Pad1.40x3.35mm_HandSolder, F.Cu at (182.6, 65.7)
- added R2: 0.05R, Resistor_SMD:R_2512_6332Metric_Pad1.40x3.35mm_HandSolder, F.Cu at (128.6, 89.7)
- added R2: 0.05R, Resistor_SMD:R_2512_6332Metric_Pad1.40x3.35mm_HandSolder, F.Cu at (128.6, 41.7)
- added R2: 0.05R, Resistor_SMD:R_2512_6332Metric_Pad1.40x3.35mm_HandSolder, F.Cu at (155.6, 89.7)
- added R2: 0.05R, Resistor_SMD:R_2512_6332Metric_Pad1.40x3.35mm_HandSolder, F.Cu at (155.6, 65.7)
- added R2: 0.05R, Resistor_SMD:R_2512_6332Metric_Pad1.40x3.35mm_HandSolder, F.Cu at (128.6, 65.7)
- added R2: 0.05R, Resistor_SMD:R_2512_6332Metric_Pad1.40x3.35mm_HandSolder, F.Cu at (182.6, 41.7)
- added R3: 47R, Resistor_SMD:R_0603_1608Metric_Pad0.98x0.95mm_HandSolder, F.Cu at (151.9, 64.8)
- added R3: 47R, Resistor_SMD:R_0603_1608Metric_Pad0.98x0.95mm_HandSolder, F.Cu at (124.9, 64.8)
- added R3: 47R, Resistor_SMD:R_0603_1608Metric_Pad0.98x0.95mm_HandSolder, F.Cu at (151.9, 88.8)
- added R3: 47R, Resistor_SMD:R_0603_1608Metric_Pad0.98x0.95mm_HandSolder, F.Cu at (178.9, 40.8)
- added R3: 47R, Resistor_SMD:R_0603_1608Metric_Pad0.98x0.95mm_HandSolder, F.Cu at (124.9, 88.8)
- added R3: 47R, Resistor_SMD:R_0603_1608Metric_Pad0.98x0.95mm_HandSolder, F.Cu at (178.9, 64.8)
- added R3: 47R, Resistor_SMD:R_0603_1608Metric_Pad0.98x0.95mm_HandSolder, F.Cu at (178.9, 88.8)
- added R3: 47R, Resistor_SMD:R_0603_1608Metric_Pad0.98x0.95mm_HandSolder, F.Cu at (124.9, 40.8)
- added R4: 47R, Resistor_SMD:R_0603_1608Metric_Pad0.98x0.95mm_HandSolder, F.Cu at (178.9, 90.7)
- added R4: 47R, Resistor_SMD:R_0603_1608Metric_Pad0.98x0.95mm_HandSolder, F.Cu at (151.9, 90.7)
- added R4: 47R, Resistor_SMD:R_0603_1608Metric_Pad0.98x0.95mm_HandSolder, F.Cu at (151.9, 66.7)
- added R4: 47R, Resistor_SMD:R_0603_1608Metric_Pad0.98x0.95mm_HandSolder, F.Cu at (124.9, 66.7)
- added R4: 47R, Resistor_SMD:R_0603_1608Metric_Pad0.98x0.95mm_HandSolder, F.Cu at (178.9, 66.7)
- added R4: 47R, Resistor_SMD:R_0603_1608Metric_Pad0.98x0.95mm_HandSolder, F.Cu at (124.9, 42.7)
- added R4: 47R, Resistor_SMD:R_0603_1608Metric_Pad0.98x0.95mm_HandSolder, F.Cu at (178.9, 42.7)
- added R4: 47R, Resistor_SMD:R_0603_1608Metric_Pad0.98x0.95mm_HandSolder, F.Cu at (124.9, 90.7)
- added REF**: NPTH, NPTH, F.Cu at (195.0, 105.0)
- added REF**: Fiducial, Fiducial, B.Cu at (105.0, 24.0)
- added REF**: Fiducial, Fiducial, B.Cu at (192.0, 106.0)
- added REF**: Fiducial, Fiducial, B.Cu at (105.0, 106.0)
- added REF**: NPTH, NPTH, F.Cu at (195.0, 25.0)
- added REF**: Fiducial, Fiducial, F.Cu at (192.0, 106.0)
- added REF**: NPTH, NPTH, F.Cu at (102.0, 25.0)
- added REF**: Fiducial, Fiducial, F.Cu at (105.0, 106.0)
- added REF**: Fiducial, Fiducial, F.Cu at (192.0, 24.0)
- added REF**: NPTH, NPTH, F.Cu at (102.0, 105.0)
- added REF**: Fiducial, Fiducial, F.Cu at (105.0, 24.0)
- added REF**: Fiducial, Fiducial, B.Cu at (192.0, 24.0)
- added U1: INA228, Package_SO:VSSOP-10_3x3mm_P0.5mm, F.Cu at (117.4, 42.5)
- added U1: INA228, Package_SO:VSSOP-10_3x3mm_P0.5mm, F.Cu at (144.4, 66.5)
- added U1: INA228, Package_SO:VSSOP-10_3x3mm_P0.5mm, F.Cu at (171.4, 42.5)
- added U1: INA228, Package_SO:VSSOP-10_3x3mm_P0.5mm, F.Cu at (117.4, 66.5)
- added U1: INA228, Package_SO:VSSOP-10_3x3mm_P0.5mm, F.Cu at (144.4, 90.5)
- added U1: INA228, Package_SO:VSSOP-10_3x3mm_P0.5mm, F.Cu at (171.4, 66.5)
- added U1: INA228, Package_SO:VSSOP-10_3x3mm_P0.5mm, F.Cu at (171.4, 90.5)
- added U1: INA228, Package_SO:VSSOP-10_3x3mm_P0.5mm, F.Cu at (117.4, 90.5)
- added U2: AMS1117/WL9005P3, Package_TO_SOT_SMD:SOT-89-3_Handsoldering, F.Cu at (172.8, 33.2)
- added U2: AMS1117/WL9005P3, Package_TO_SOT_SMD:SOT-89-3_Handsoldering, F.Cu at (172.8, 81.2)
- added U2: AMS1117/WL9005P3, Package_TO_SOT_SMD:SOT-89-3_Handsoldering, F.Cu at (118.8, 57.2)
- added U2: AMS1117/WL9005P3, Package_TO_SOT_SMD:SOT-89-3_Handsoldering, F.Cu at (118.8, 33.2)
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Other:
- board size 102.6 x 93.3 mm -> 105 x 96 mm
